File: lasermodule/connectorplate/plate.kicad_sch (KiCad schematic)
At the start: 2 parts, among them J1 292173-5, J2 Conn_01x05

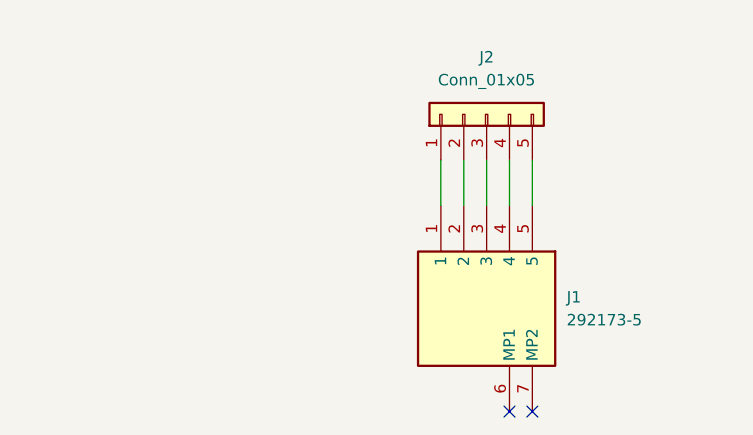
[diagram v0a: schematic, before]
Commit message: added kicost tracking other plates, fixed plates
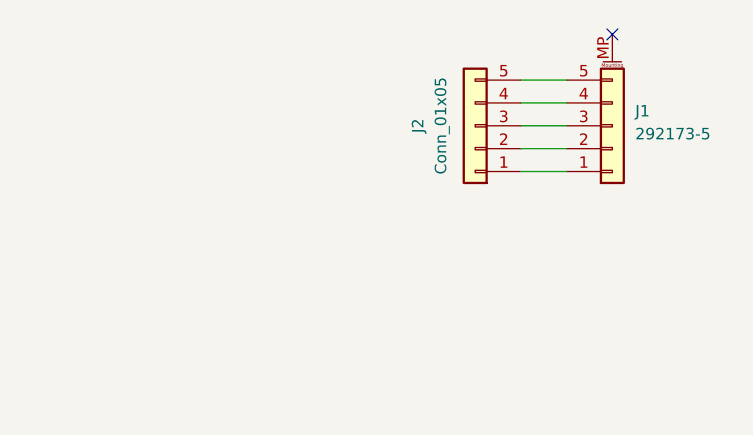
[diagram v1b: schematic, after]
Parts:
- J1: symbol mirrormotor:292173-5 -> Connector_Generic_MountingPin:Conn_01x05_MountingPin; Height 6.1 -> (none); Manufacturer_Name TE Connectivity -> (none); Manufacturer_Part_Number 292173-5 -> (none); Mouser Part Number 571-292173-5 -> (none); Mouser Price/Stock https://www.mouser.co.uk/ProductDetail/TE-Connectivity-Alco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 -> (none)
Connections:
- no-connect marks 2 -> 1
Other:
- moved on the sheet: J2
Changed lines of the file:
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@@
 	(paper "A4")
 	(no_connect
-		(at 100.33 123.19)
-	)
-	(no_connect
-		(at 97.79 123.19)
+		(at 109.22 81.28)
 	)
 	(wire
 		(pts
-			(xy 95.25 95.25) (xy 95.25 100.33)
+			(xy 99.06 91.44) (xy 104.14 91.44)
 		)
 		(stroke
@@
 	(wire
 		(pts
-			(xy 100.33 95.25) (xy 100.33 100.33)
+			(xy 99.06 86.36) (xy 104.14 86.36)
 		)
 		(stroke
@@
 	(wire
 		(pts
-			(xy 92.71 95.25) (xy 92.71 100.33)
+			(xy 99.06 93.98) (xy 104.14 93.98)
 		)
 		(stroke
@@
 	(wire
 		(pts
-			(xy 97.79 95.25) (xy 97.79 100.33)
+			(xy 99.06 88.9) (xy 104.14 88.9)
 		)
 		(stroke
@@
 	(wire
 		(pts
-			(xy 90.17 95.25) (xy 90.17 100.33)
+			(xy 99.06 96.52) (xy 104.14 96.52)
 		)
 		(stroke
@@
 	)
 	(symbol
-		(lib_id "mirrormotor:292173-5")
-		(at 100.33 100.33 270)
+		(lib_id "Connector_Generic_MountingPin:Conn_01x05_MountingPin")
+		(at 109.22 91.44 0)
+		(mirror x)
 		(unit 1)
 		(exclude_from_sim no)
@@
 		(fields_autoplaced yes)
 		(property "Reference" "J1"
-			(at 104.14 110.4899 90)
+			(at 111.76 89.8143 0)
 			(effects
 				(font
@@
 		)
 		(property "Value" "292173-5"
-			(at 104.14 113.0299 90)
+			(at 111.76 92.3543 0)
 			(effects
 				(font
@@
 		)
 		(property "Footprint" "mirrormotor:2921735"
-			(at 5.41 119.38 0)
-			(effects
-				(font
-					(size 1.27 1.27)
-				)
-				(justify left top)
-				(hide yes)
-			)
-		)
-		(property "Datasheet" "https://www.te.com/commerce/DocumentDelivery/DDEController?Action=srchrtrv&DocNm=292173&DocType=Customer+Drawing&DocLang=English"
-			(at -94.59 119.38 0)
-			(effects
-				(font
-					(size 1.27 1.27)
-				)
-				(justify left top)
-				(hide yes)
-			)
-		)
-		(property "Description" "PCB Mount Header, Right Angle, Wire-to-Board, 5 Position, 2 mm [.079 in] Centerline, Partially Shrouded, Tin, Surface Mount, Power & Signal, AMP CT"
-			(at 100.33 100.33 0)
+			(at 109.22 91.44 0)
 			(effects
 				(font
@@
 			)
 		)
-		(property "Height" "6.1"
-			(at -294.59 119.38 0)
+		(property "Datasheet" "~"
+			(at 109.22 91.44 0)
 			(effects
 				(font
 					(size 1.27 1.27)
 				)
-				(justify left top)
 				(hide yes)
 			)
 		)
-		(property "Mouser Part Number" "571-292173-5"
-			(at -394.59 119.38 0)
+		(property "Description" "Generic connectable mounting pin connector, single row, 01x05, script generated (kicad-library-utils/schlib/autogen/connector/)"
+			(at 109.22 91.44 0)
 			(effects
 				(font
 					(size 1.27 1.27)
 				)
-				(justify left top)
-				(hide yes)
-			)
-		)
-		(property "Mouser Price/Stock" "https://www.mouser.co.uk/ProductDetail/TE-Connectivity-Alcoswitch/292173-5?qs=cTq9ZV%252BpM4%252BzH2IkFejNJQ%3D%3D"
-			(at -494.59 119.38 0)
-			(effects
-				(font
-					(size 1.27 1.27)
-				)
-				(justify left top)
-				(hide yes)
-			)
-		)
-		(property "Manufacturer_Name" "TE Connectivity"
-			(at -594.59 119.38 0)
-			(effects
-				(font
-					(size 1.27 1.27)
-				)
-				(justify left top)
-				(hide yes)
-			)
-		)
-		(property "Manufacturer_Part_Number" "292173-5"
-			(at -694.59 119.38 0)
-			(effects
-				(font
-					(size 1.27 1.27)
-				)
-				(justify left top)
 				(hide yes)
 			)
@@
 		(pin "4"
 		)
-		(pin "6"
+		(pin "MP"
 		)
 		(pin "3"
@@
 		)
 		(pin "5"
-		)
-		(pin "7"
 		)
 		(instances
@@
 	(symbol
 		(lib_id "Connector_Generic:Conn_01x05")
-		(at 95.25 90.17 90)
+		(at 93.98 91.44 180)
 		(unit 1)
 		(exclude_from_sim no)
@@
 		(fields_autoplaced yes)
 		(property "Reference" "J2"
-			(at 95.25 83.82 90)
+			(at 87.63 91.44 90)
 			(effects
 				(font
@@
 		)
 		(property "Value" "Conn_01x05"
-			(at 95.25 86.36 90)
+			(at 90.17 91.44 90)
 			(effects
 				(font
@@
 		)
 		(property "Footprint" "mirrormotor:PinHeader_1x05_P2.00mm_Vertical"
-			(at 95.25 90.17 0)
+			(at 93.98 91.44 0)
 			(effects
 				(font
@@
 		)
 		(property "Datasheet" "~"
-			(at 95.25 90.17 0)
+			(at 93.98 91.44 0)
 			(effects
 				(font
@@
 		)
 		(property "Description" "Generic connector, single row, 01x05, script generated (kicad-library-utils/schlib/autogen/connector/)"
-			(at 95.25 90.17 0)
+			(at 93.98 91.44 0)
 			(effects
 				(font

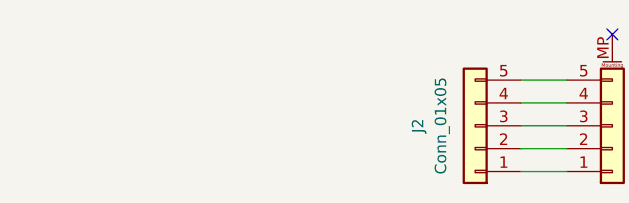
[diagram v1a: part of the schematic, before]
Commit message: fixed boms, small modifications to the boards.
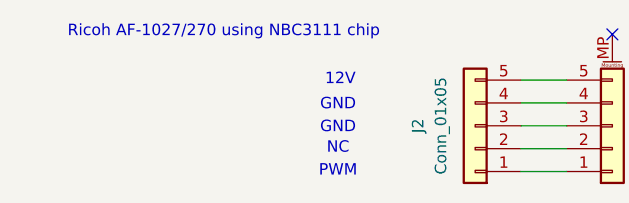
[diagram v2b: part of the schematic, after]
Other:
- note added: "12V"
- note added: "GND"
- note added: "NC"
- note added: "PWM"
- note added: "Ricoh AF-1027/270 using NBC3111 chip"
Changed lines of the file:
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@@
+		)
+	)
+	(text "GND\n"
+		(exclude_from_sim no)
+		(at 78.74 91.694 0)
+		(effects
+			(font
+				(size 1.27 1.27)
+			)
+		)
+	)
+	(text "12V"
+		(exclude_from_sim no)
+		(at 78.994 86.36 0)
+		(effects
+			(font
+				(size 1.27 1.27)
+			)
+		)
+	)
+	(text "Ricoh AF-1027/270 using NBC3111 chip"
+		(exclude_from_sim no)
+		(at 66.04 81.026 0)
+		(effects
+			(font
+				(size 1.27 1.27)
+			)
+		)
+	)
+	(text "PWM"
+		(exclude_from_sim no)
+		(at 78.74 96.52 0)
+		(effects
+			(font
+				(size 1.27 1.27)
+			)
+		)
+	)
+	(text "GND\n"
+		(exclude_from_sim no)
+		(at 78.74 89.154 0)
+		(effects
+			(font
+				(size 1.27 1.27)
+			)
+		)
+	)
+	(text "NC"
+		(exclude_from_sim no)
+		(at 78.74 93.98 0)
+		(effects
+			(font
+				(size 1.27 1.27)
+			)
 		)
 	)
